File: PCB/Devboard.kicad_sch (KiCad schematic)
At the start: 0 parts

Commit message: Refactor : Repo
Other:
- sheet Expansion: file schematics\12_Expansion\12_Expansion.kicad_sch -> schematics/12_Expansion/12_Expansion.kicad_sch
- sheet Harvester, BMC, Telemetry: file schematics\10_Harvester_BMC_Telemetry\10_Harvester_BMC_Telemetry.kicad_sch -> schematics/10_Harvester_BMC_Telemetry/10_Harvester_BMC_Telemetry.kicad_sch
- sheet RTC & Security: file schematics\09_RTC_Security\09_RTC_Security.kicad_sch -> schematics/09_RTC_Security/09_RTC_Security.kicad_sch
- sheet Sensors and GNSS: file schematics\08_Sensors_GNSS\08_Sensors_GNSS.kicad_sch -> schematics/08_Sensors_GNSS/08_Sensors_GNSS.kicad_sch
- sheet ePaper Ink Display: file schematics\11_ePaper\11_ePaper.kicad_sch -> schematics/11_ePaper/11_ePaper.kicad_sch
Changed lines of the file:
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@@
 		(stroke
 			(width 0)
-			(type default)
-		)
-		(fill
-			(type none)
+			(type solid)
+		)
+		(fill
+			(type color)
+			(color 255 229 191 1)
 		)
 	)
@@
 		)
 	)
-	(text_box "Author : Hemanth\nYSWS : Pixl"
+	(text_box "Author : Hemanth\nYSWS : Pixl\n"
 		(exclude_from_sim no)
 		(at 12.065 12.065 0)
@@
 			)
 		)
-		(property "Sheetfile" "schematics\\11_ePaper\\11_ePaper.kicad_sch"
+		(property "Sheetfile" "schematics/11_ePaper/11_ePaper.kicad_sch"
 			(at 197.485 348.5646 0)
 			(show_name no)
@@
 			)
 		)
-		(property "Sheetfile" "schematics\\12_Expansion\\12_Expansion.kicad_sch"
+		(property "Sheetfile" "schematics/12_Expansion/12_Expansion.kicad_sch"
 			(at 298.45 348.5646 0)
 			(show_name no)
@@
 			)
 		)
-		(property "Sheetfile" "schematics\\08_Sensors_GNSS\\08_Sensors_GNSS.kicad_sch"
+		(property "Sheetfile" "schematics/08_Sensors_GNSS/08_Sensors_GNSS.kicad_sch"
 			(at 248.92 253.3146 0)
 			(show_name no)
@@
 			)
 		)
-		(property "Sheetfile" "schematics\\09_RTC_Security\\09_RTC_Security.kicad_sch"
+		(property "Sheetfile" "schematics/09_RTC_Security/09_RTC_Security.kicad_sch"
 			(at 349.25 253.3146 0)
 			(show_name no)
@@
 			)
 		)
-		(property "Sheetfile" "schematics\\10_Harvester_BMC_Telemetry\\10_Harvester_BMC_Telemetry.kicad_sch"
+		(property "Sheetfile" "schematics/10_Harvester_BMC_Telemetry/10_Harvester_BMC_Telemetry.kicad_sch"
 			(at 445.77 253.3146 0)
 			(show_name no)

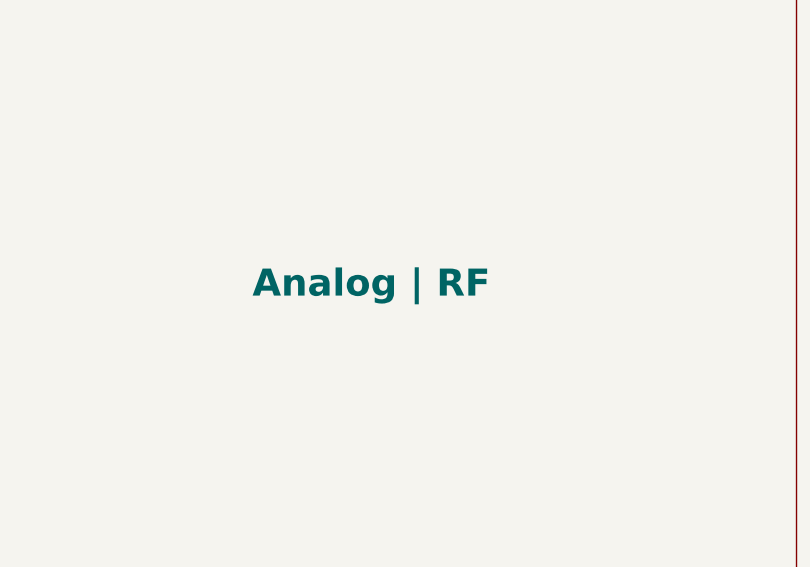
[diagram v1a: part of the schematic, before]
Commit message: Added Schematic Images
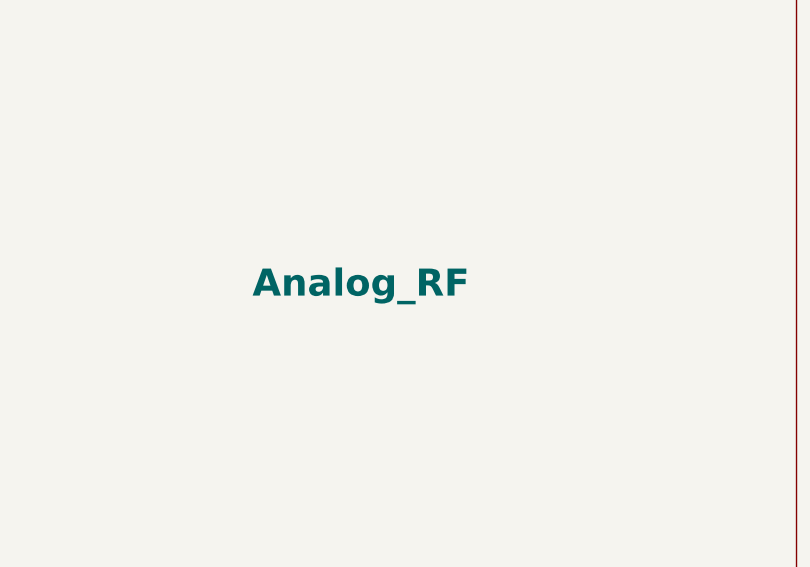
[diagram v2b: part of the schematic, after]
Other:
- sheet Analog | RF renamed Analog_RF
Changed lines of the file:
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@@
 			(color 0 0 0 0)
 		)
-		(property "Sheetname" "Analog | RF"
+		(property "Sheetname" "Analog_RF"
 			(at 173.228 215.138 0)
 			(show_name no)
